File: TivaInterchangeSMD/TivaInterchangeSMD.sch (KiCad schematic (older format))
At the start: 5 parts, among them J1 TI_BOOSTER_40_J1, J2 TI_BOOSTER_40_J2, J3 TI_BOOSTER_40_J3, J4 TI_BOOSTER_40_J4, P3 CONN_10

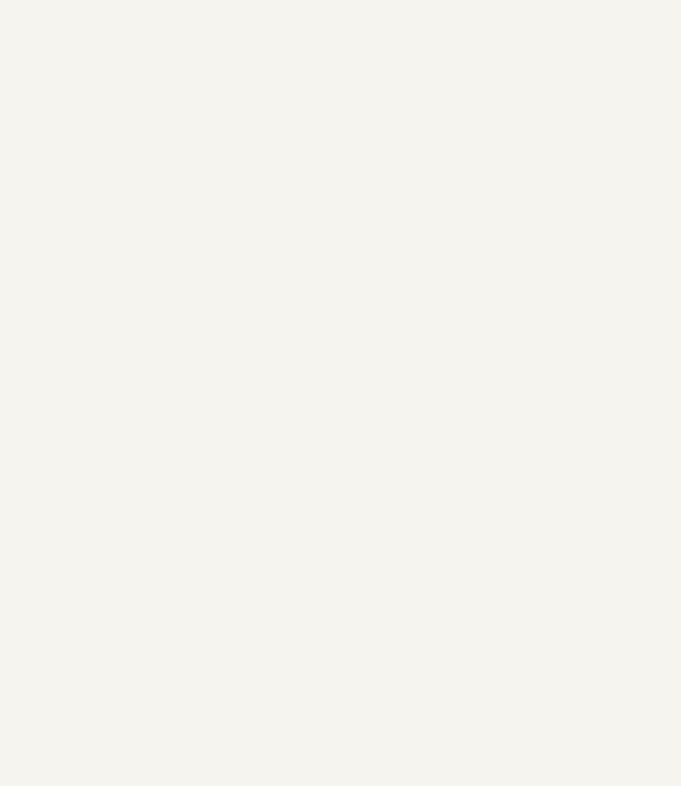
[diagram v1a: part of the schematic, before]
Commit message: Start on CAN Tranceiver boosterpack.
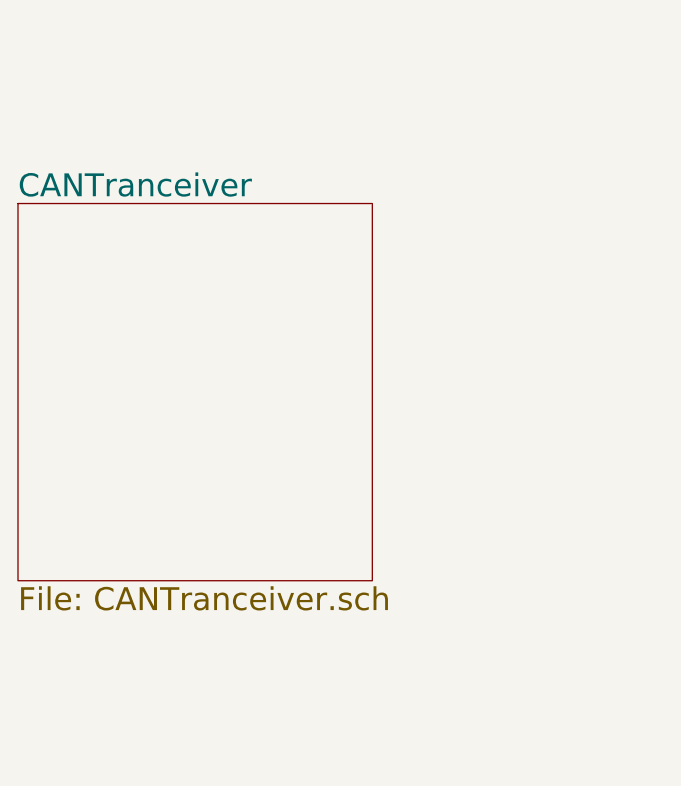
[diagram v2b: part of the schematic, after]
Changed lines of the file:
@@
 $Descr USLetter 11000 8500
 encoding utf-8
-Sheet 1 3
+Sheet 1 4
 Title "Tiva Interchange"
 Date "10 mar 2018"
@@
 Wire Wire Line
 	8500 6000 8500 6050
+$Sheet
+S 2550 3750 1550 1650
+U 5AA46B1E
+F0 "CANTranceiver" 100
+F1 "CANTranceiver.sch" 100
+$EndSheet
 $EndSCHEMATC

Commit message: Complete CAN Tranceiver board.
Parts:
- added JB1: TI_BOOSTER_40_J1, symbol TI_BOOSTER_40_J1
- added JB2: TI_BOOSTER_40_J2, symbol TI_BOOSTER_40_J2
- added JB3: TI_BOOSTER_40_J3, symbol TI_BOOSTER_40_J3
- added JB4: TI_BOOSTER_40_J4, symbol TI_BOOSTER_40_J4
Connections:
- net labels added: J3.10, J3.7, J3.8, J3.9, J4.10, J4.7, J4.8, J4.9
- wire segments 37 -> 43
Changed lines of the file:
@@
 Sheet 1 4
 Title "Tiva Interchange"
-Date "10 mar 2018"
+Date "11 mar 2018"
 Rev "1.0"
 Comp "Deepwoods Software"
@@
 $EndSheet
 $Sheet
-S 5750 800  1600 1850
+S 6350 2400 1600 1300
 U 5AA03023
 F0 "QuadSignalHead" 100
 F1 "QuadSignalHead.sch" 100
-F2 "SCL" I R 7350 1100 60
-F3 "SDA" B R 7350 1450 60
+F2 "SCL" I R 7950 2700 60
+F3 "SDA" B R 7950 3050 60
 $EndSheet
 $Comp
@@
 $EndComp
 Wire Wire Line
-	7350 1100 8650 1100
-Wire Wire Line
-	8650 1100 8650 1700
-Wire Wire Line
-	8650 1700 9150 1700
-Wire Wire Line
-	9150 1800 8150 1800
-Wire Wire Line
-	8150 1800 8150 1450
-Wire Wire Line
-	8150 1450 7350 1450
-Wire Wire Line
 	9150 4200 7850 4200
 Wire Wire Line
@@
 Wire Wire Line
 	8500 6000 8500 6050
+Wire Wire Line
+	7950 3050 8700 3050
+Wire Wire Line
+	8700 3050 8700 1800
+Wire Wire Line
+	8700 1800 9150 1800
+Wire Wire Line
+	7950 2700 8500 2700
+Wire Wire Line
+	8500 2700 8500 1700
+Wire Wire Line
+	8500 1700 9150 1700
+Text GLabel 8550 6500 0    60   Input ~ 0
+J4.10
+Text GLabel 8800 6400 0    60   Input ~ 0
+J4.9
+Text GLabel 8500 6300 0    60   Input ~ 0
+J4.8
+Text GLabel 8800 6200 0    60   Input ~ 0
+J4.7
+Text GLabel 8550 4900 0    60   Input ~ 0
+J3.10
+Text GLabel 8950 4800 0    60   Input ~ 0
+J3.9
+Text GLabel 8500 4700 0    60   Input ~ 0
+J3.8
+Text GLabel 8850 4600 0    60   Input ~ 0
+J3.7
+$Comp
+L VCC #PWR08
+U 1 1 5AA6180F
+P 2650 1000
+F 0 "#PWR08" H 2650 1100 30  0001 C CNN
+F 1 "VCC" H 2650 1100 30  0000 C CNN
+F 2 "" H 2650 1000 60  0001 C CNN
+F 3 "" H 2650 1000 60  0001 C CNN
+	1    2650 1000
+	0    -1   -1   0
+$EndComp
+$Comp
+L TI_BOOSTER_40_J1 JB1
+U 1 1 5AA61815
+P 3250 1450
+F 0 "JB1" H 3200 2100 60  0000 C CNN
+F 1 "TI_BOOSTER_40_J1" H 3250 800 60  0000 C CNN
+F 2 "" H 3250 1450 60  0001 C CNN
+F 3 "" H 3250 1450 60  0001 C CNN
+	1    3250 1450
+	1    0    0    -1
+$EndComp
+$Comp
+L TI_BOOSTER_40_J2 JB2
+U 1 1 5AA6181B
+P 3250 3000
+F 0 "JB2" H 3200 3650 60  0000 C CNN
+F 1 "TI_BOOSTER_40_J2" H 3250 2350 60  0000 C CNN
+F 2 "" H 3250 3000 60  0001 C CNN
+F 3 "" H 3250 3000 60  0001 C CNN
+	1    3250 3000
+	1    0    0    -1
+$EndComp
+$Comp
+L TI_BOOSTER_40_J3 JB3
+U 1 1 5AA61821
+P 3250 4550
+F 0 "JB3" H 3200 5200 60  0000 C CNN
+F 1 "TI_BOOSTER_40_J3" H 3250 3900 60  0000 C CNN
+F 2 "" H 3250 4550 60  0001 C CNN
+F 3 "" H 3250 4550 60  0001 C CNN
+	1    3250 4550
+	1    0    0    -1
+$EndComp
+$Comp
+L TI_BOOSTER_40_J4 JB4
+U 1 1 5AA61827
+P 3250 6100
+F 0 "JB4" H 3200 6750 60  0000 C CNN
+F 1 "TI_BOOSTER_40_J4" H 3250 5450 60  0000 C CNN
+F 2 "" H 3250 6100 60  0001 C CNN
+F 3 "" H 3250 6100 60  0001 C CNN
+	1    3250 6100
+	1    0    0    -1
+$EndComp
+$Comp
+L GND #PWR09
+U 1 1 5AA6182D
+P 2650 4200
+F 0 "#PWR09" H 2650 4200 30  0001 C CNN
+F 1 "GND" H 2650 4130 30  0001 C CNN
+F 2 "" H 2650 4200 60  0001 C CNN
+F 3 "" H 2650 4200 60  0001 C CNN
+	1    2650 4200
+	0    1    1    0
+$EndComp
 $Sheet
-S 2550 3750 1550 1650
+S 650  900  1550 1650
 U 5AA46B1E
 F0 "CANTranceiver" 100
 F1 "CANTranceiver.sch" 100
+F2 "CAN Rx" I R 2200 1100 60
+F3 "CAN Tx" I R 2200 1250 60
 $EndSheet
+Wire Wire Line
+	2200 1250 2450 1250
+Wire Wire Line
+	2450 1250 2450 1500
+Wire Wire Line
+	2450 1500 2650 1500
+Wire Wire Line
+	2650 1400 2500 1400
+Wire Wire Line
+	2500 1400 2500 1100
+Wire Wire Line
+	2500 1100 2200 1100
 $EndSCHEMATC

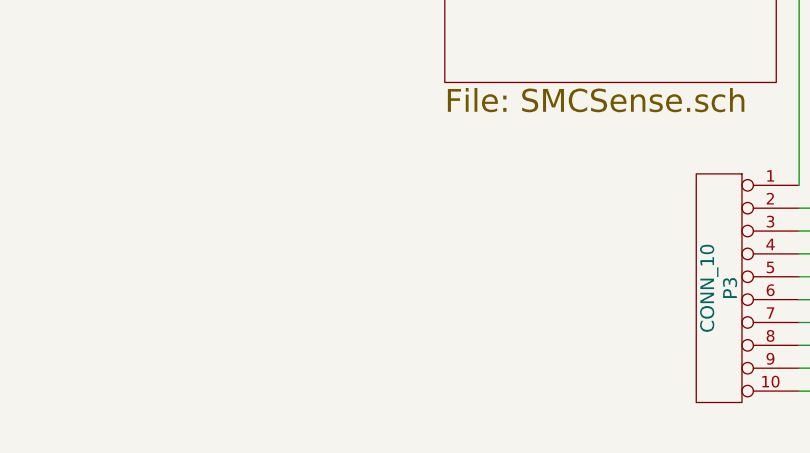
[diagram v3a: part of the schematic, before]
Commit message: Add connection breakout boards.
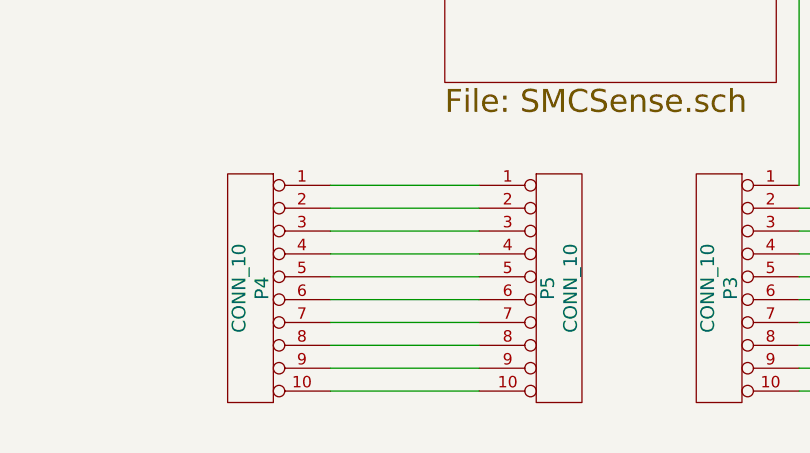
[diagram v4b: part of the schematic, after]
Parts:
- added P4: CONN_10, ScrewTerm_2.54-10, symbol CONN_10
- added P5: CONN_10, PIN_ARRAY_5x2, symbol CONN_10
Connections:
- wire segments 43 -> 53
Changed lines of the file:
@@
 Sheet 1 4
 Title "Tiva Interchange"
-Date "11 mar 2018"
+Date "12 mar 2018"
 Rev "1.0"
 Comp "Deepwoods Software"
@@
 Wire Wire Line
 	2500 1100 2200 1100
+$Comp
+L CONN_10 P5
+U 1 1 5AA67269
+P 6900 6050
+AR Path="/5AA67269" Ref="P5"  Part="1"
+AR Path="/5AA03023/5AA67269" Ref="P?"  Part="1"
+F 0 "P5" V 6850 6050 60  0000 C CNN
+F 1 "CONN_10" V 6950 6050 60  0000 C CNN
+F 2 "PIN_ARRAY_5x2" H 6900 6050 60  0001 C CNN
+F 3 "~" H 6900 6050 60  0000 C CNN
+	1    6900 6050
+	1    0    0    -1
+$EndComp
+$Comp
+L CONN_10 P4
+U 1 1 5AA67290
+P 5550 6050
+F 0 "P4" V 5500 6050 60  0000 C CNN
+F 1 "CONN_10" V 5600 6050 60  0000 C CNN
+F 2 "ScrewTerm_2.54-10" H 5550 6050 60  0001 C CNN
+F 3 "~" H 5550 6050 60  0000 C CNN
+	1    5550 6050
+	-1   0    0    -1
+$EndComp
+Wire Wire Line
+	5900 6500 6550 6500
+Wire Wire Line
+	5900 6400 6550 6400
+Wire Wire Line
+	5900 6300 6550 6300
+Wire Wire Line
+	5900 6200 6550 6200
+Wire Wire Line
+	5900 6100 6550 6100
+Wire Wire Line
+	5900 6000 6550 6000
+Wire Wire Line
+	5900 5900 6550 5900
+Wire Wire Line
+	5900 5800 6550 5800
+Wire Wire Line
+	5900 5700 6550 5700
+Wire Wire Line
+	5900 5600 6550 5600
 $EndSCHEMATC
